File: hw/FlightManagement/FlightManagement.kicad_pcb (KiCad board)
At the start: 2 copper layers, 50 x 50 mm, 116 parts, among them J1 BWSMA-KE-Z001, J2 B4B-EH-A(LF)(SN), J3 B6B-EH-A(LF)(SN), J5 Conn_01x24_MountingPin, J6 Conn_01x02_Socket, J7 Conn_01x02_Pin, U1 YTS1C0033BBG01, U12 TPS54202DDC, U14 SN74LVC1G125DBV, U15 SN74LVC1G125DBV, U2 STM32L431RCTx, U3 MPU-6050, U4 LIS2MDL, U6 XA17-G4K, U8 SN65HVD230, U9 W25Q128JVS, Y1 13.56 MHz, Y2 10.7 MHz, Y3 6.6128 MHz, Y4 Crystal_GND24

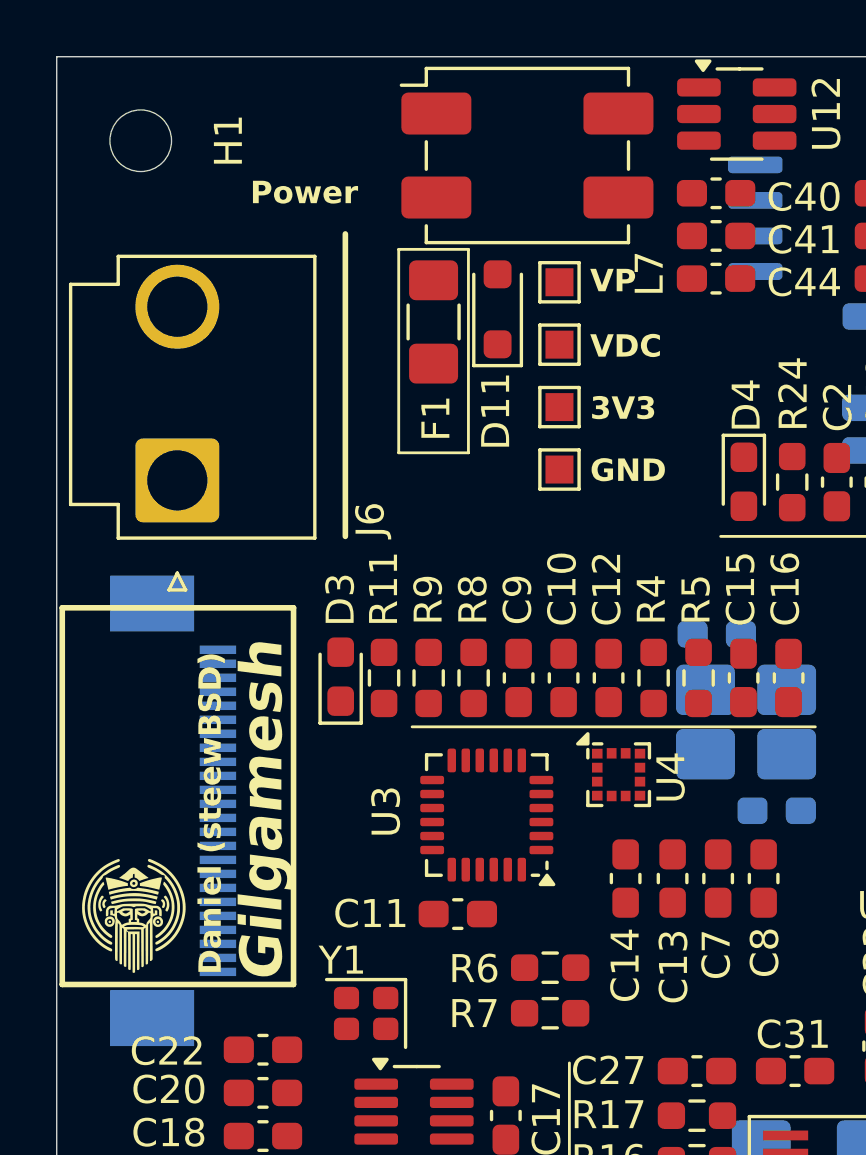
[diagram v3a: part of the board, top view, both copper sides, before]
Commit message: preliminar design for battery power monitor, add sd card to fmu
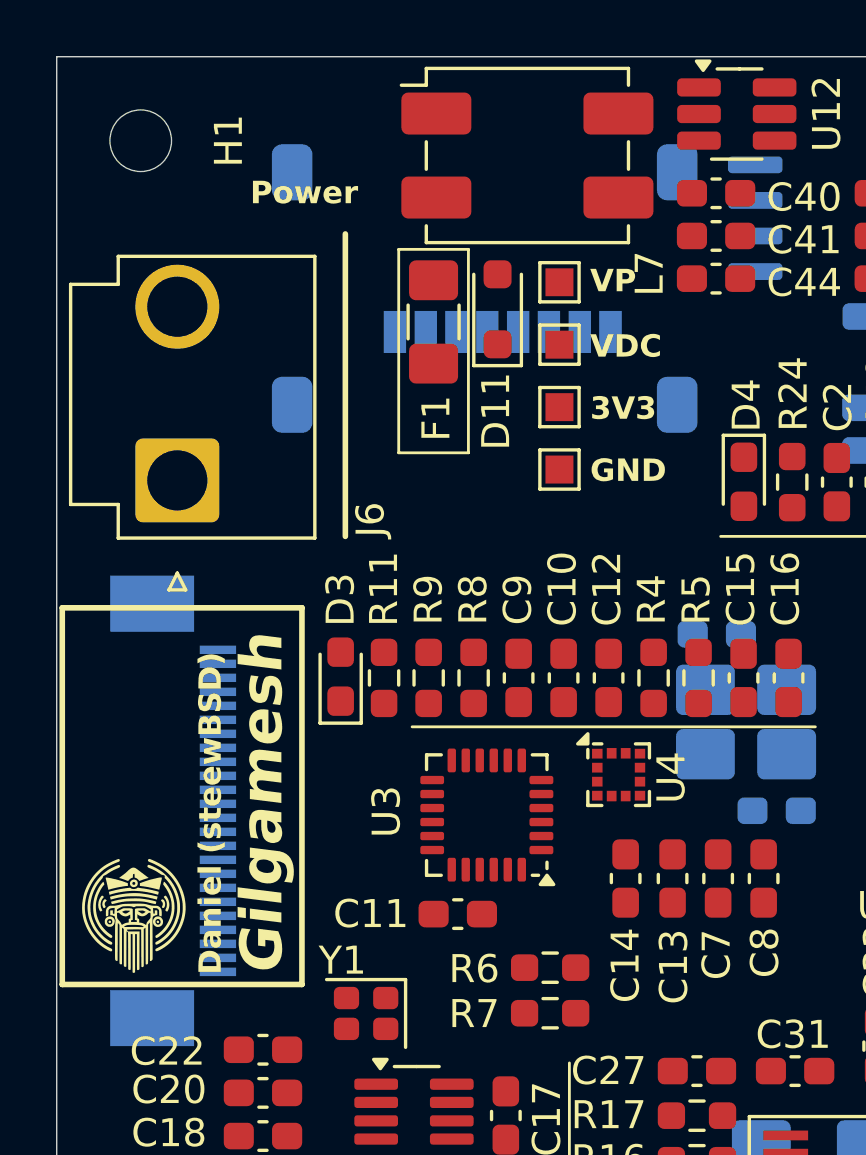
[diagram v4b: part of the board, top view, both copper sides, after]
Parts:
- added J4: Micro_SD_Card, Connector_Card:microSD_HC_Molex_47219-2001, B.Cu at (127.6, 85.2)
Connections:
- U2 pad 10: /AGCDIS -> /CAMERA2
- U2 pad 11: unconnected-(U2-PC3-Pad11) -> /CAMERA3
- U2 pad 14: unconnected-(U2-PA0-Pad14) -> /SDCD
- U2 pad 20: unconnected-(U2-PA4-Pad20) -> /CAMERA1
- U2 pad 21: unconnected-(U2-PA5-Pad21) -> /CAMERA0
- U2 pad 33: /CAMERA3 -> unconnected-(U2-PB12-Pad33)
- U2 pad 34: /CAMERA2 -> /SDSCK
- U2 pad 35: /CAMERA1 -> /SDMISO
- U2 pad 36: /CAMERA0 -> /SDMOSI
- U2 pad 54: unconnected-(U2-PD2-Pad54) -> /AGCDIS

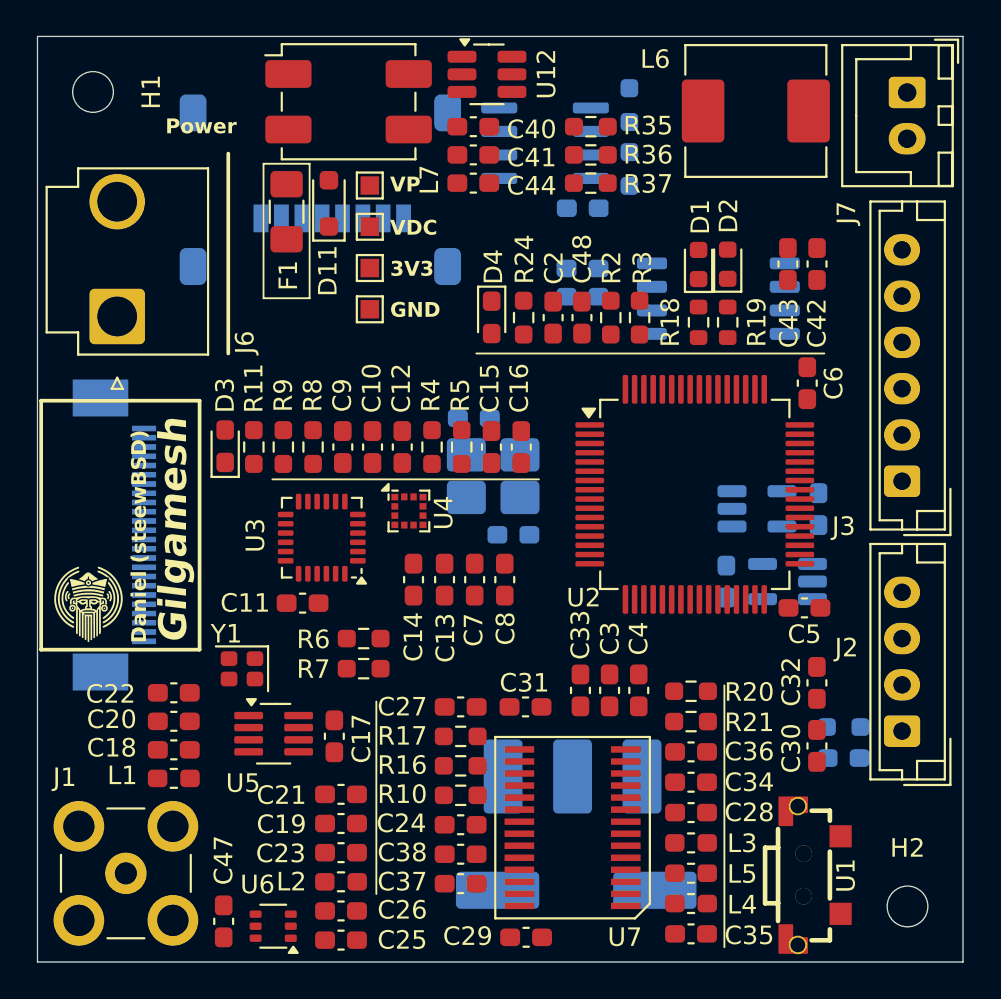
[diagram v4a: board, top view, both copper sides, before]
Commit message: make fmu pcb more organized
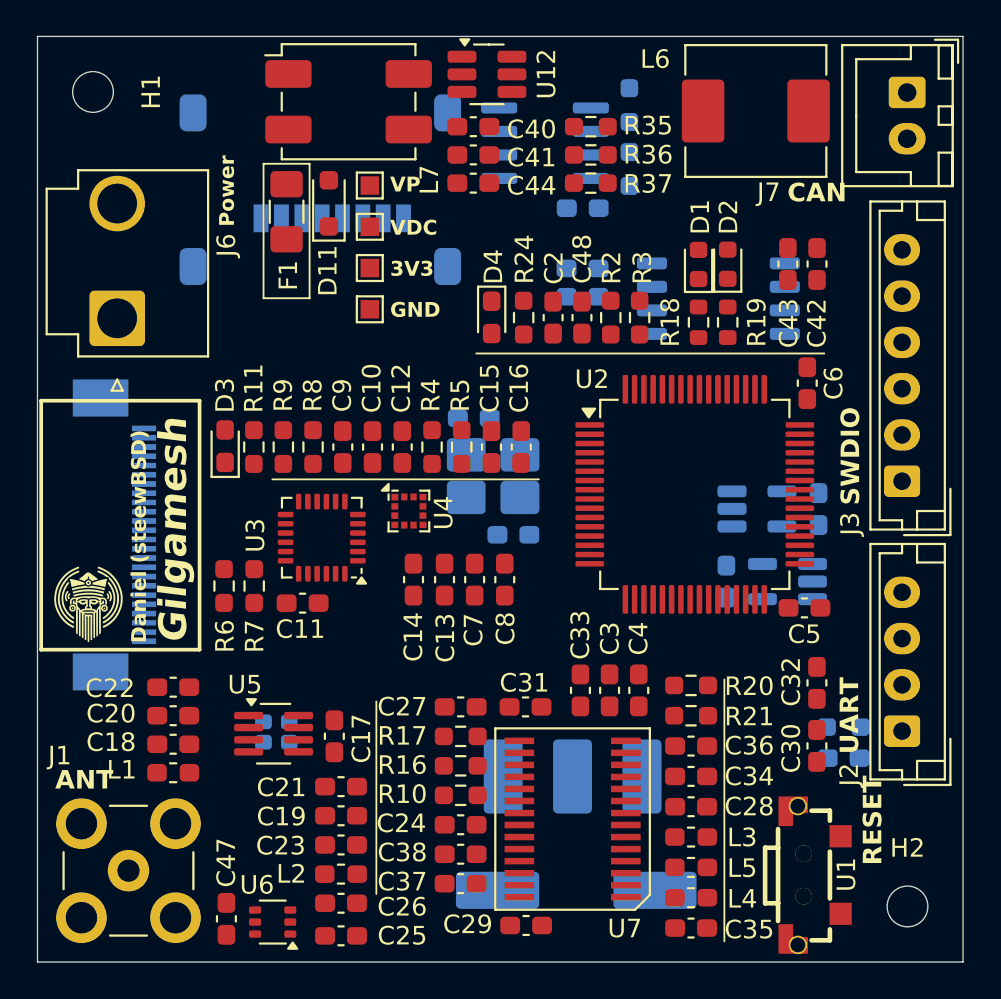
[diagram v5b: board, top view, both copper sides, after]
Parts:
- Y1: moved to B.Cu
- moved R6 8.06 mm to (122.4, 107.2), turned to 90 degrees
- moved R7 7.41 mm to (124.0, 107.2), turned to 90 degrees
- moved Y1 3.89 mm to (125.2, 115.0)
- moved C29 0.64 mm to (138.7, 125.5)
- moved U7 0.47 mm to (141.2, 119.8)
- moved C19 0.42 mm to (128.7, 119.6)
- moved C21 0.42 mm to (128.7, 118.0)
- moved C26 0.42 mm to (128.7, 124.3)
- moved C23 0.42 mm to (128.7, 121.1)
- moved L2 0.42 mm to (128.7, 122.7)
- moved C28 0.31 mm to (147.6, 119.1)
- moved C34 0.31 mm to (147.6, 117.4)
- moved C36 0.31 mm to (147.6, 115.8)
- moved L3 0.31 mm to (147.6, 120.7)
- moved R20 0.31 mm to (147.6, 112.5)
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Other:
- board text added: "ANT"
- board text added: "CAN"
- board text added: "FFC"
- board text added: "MICROSD"
- board text added: "RESET"
- board text added: "SWDIO"
- board text added: "UART"

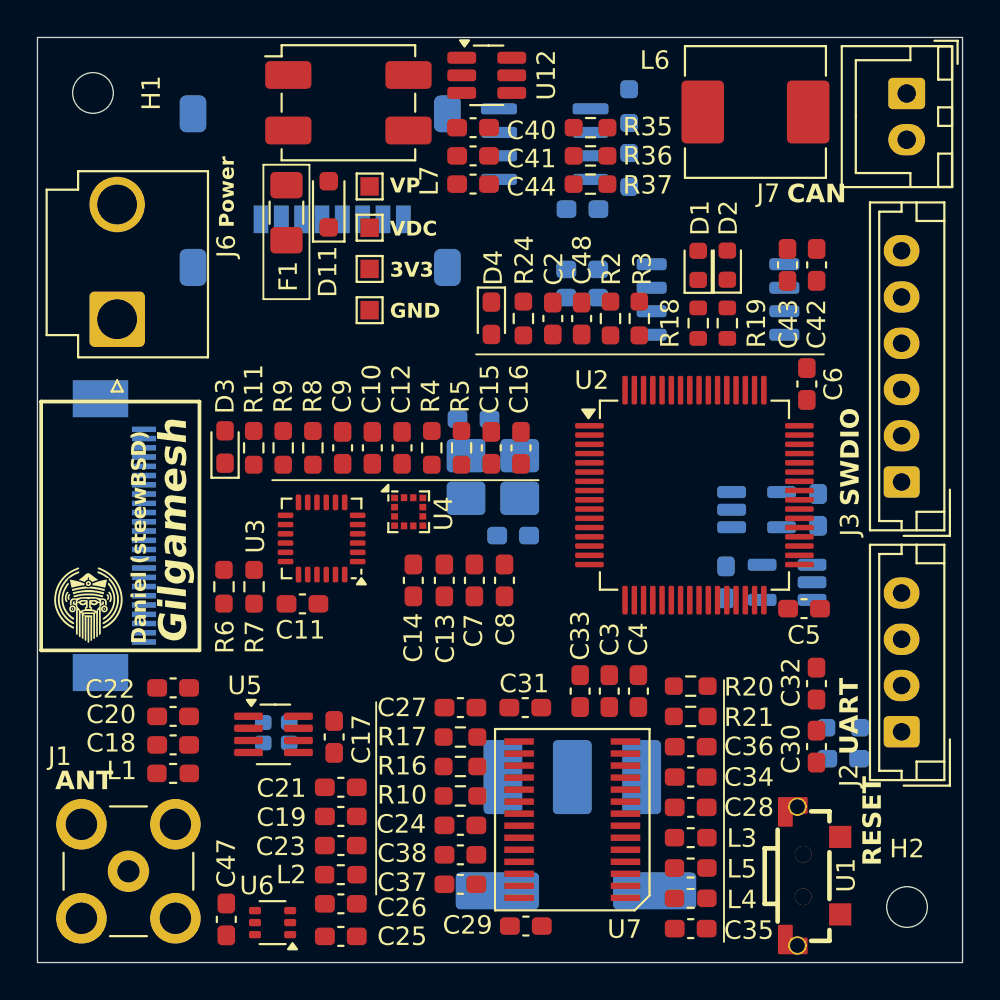
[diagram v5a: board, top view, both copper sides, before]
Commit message: finish fmu routing
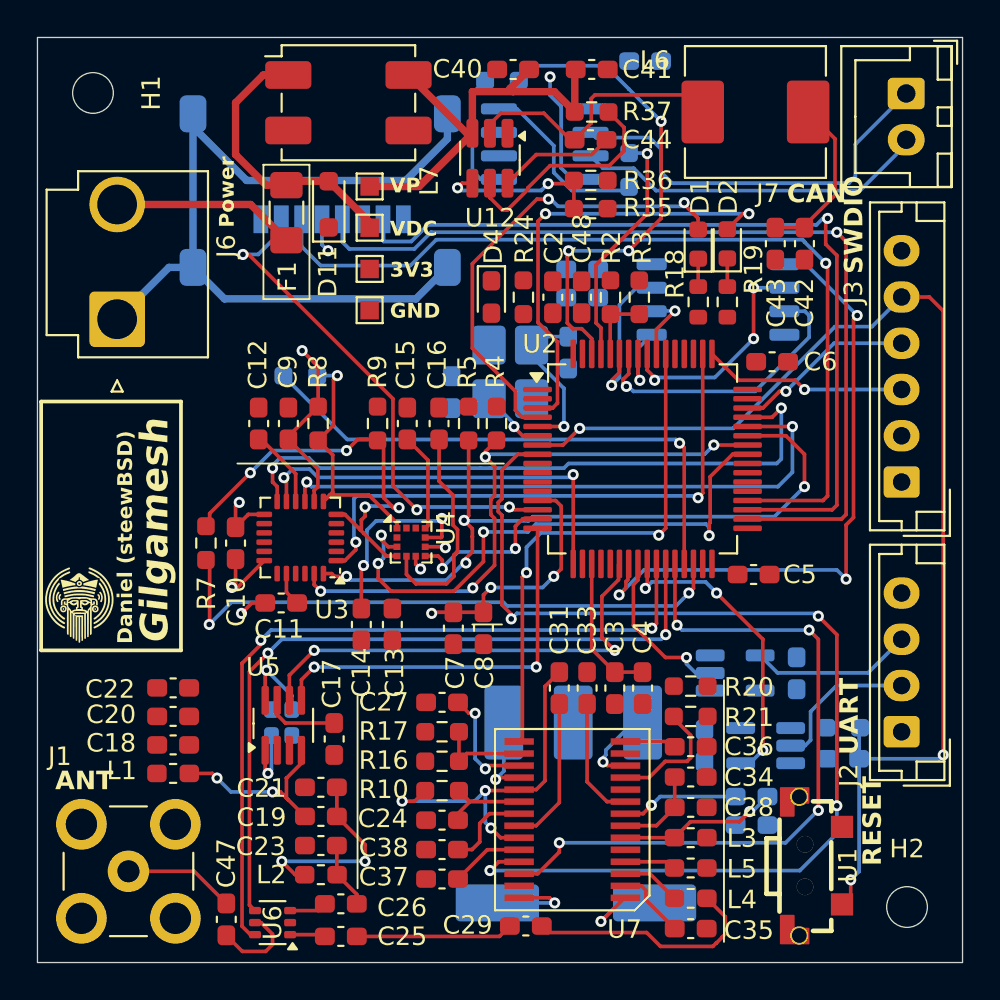
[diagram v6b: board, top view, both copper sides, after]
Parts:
- removed D3: KT-0603W, LED_SMD:LED_0603_1608Metric_Pad1.05x0.95mm_HandSolder
- removed J5: Conn_01x24_MountingPin, Connector_FFC-FPC:Jushuo_AFC07-S24FCA-00_1x24-1MP_P0.50_Horizontal
- removed R11: 1 kOhm, Resistor_SMD:R_0603_1608Metric_Pad0.98x0.95mm_HandSolder
- C30, C32, R6: moved to B.Cu
- moved R6 12.1 mm to (126.5, 95.8), turned to 0 degrees
- moved C10 9.01 mm to (123.0, 104.8), turned to 90 degrees
- moved C50 8.91 mm to (153.3, 111.8)
- moved U14 8.91 mm to (151.7, 115.8)
- moved U15 8.91 mm to (150.0, 111.8)
- moved C49 8.91 mm to (148.3, 115.8)
- moved C39 8.69 mm to (145.1, 78.8)
- moved C46 8.43 mm to (134.7, 96.6), turned to -90 degrees
- moved C41 7.93 mm to (142.2, 79.2)
- moved C12 7.86 mm to (124.2, 98.3)
- moved U5 7.34 mm to (119.9, 114.8), turned to 90 degrees
- moved C32 7.04 mm to (150.9, 118.5), turned to 0 degrees
- moved R12 7.01 mm to (137.4, 79.8), turned to 180 degrees
- moved C44 6.79 mm to (142.2, 83.0)
- moved C45 6.25 mm to (141.0, 94.5), turned to 90 degrees
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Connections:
- net Net-(J6-Pin_2) renamed /VDCPRE
- net Net-(U12-VIN) renamed /VIN
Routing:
- net +3V3: track 0.00 -> 80.6 mm, vias 0 -> 8
- net /NRESET: track 0.00 -> 64.1 mm, vias 0 -> 3
- net /DATAOUT: track 0.00 -> 61.0 mm, vias 0 -> 4
- net /SDSCK: track 0.00 -> 49.4 mm, vias 0 -> 1
- net /SDMOSI: track 0.00 -> 48.4 mm, vias 0 -> 1
- net GNDPWR: track 0.00 -> 46.7 mm
- net /SDMISO: track 0.00 -> 46.4 mm, vias 0 -> 1
- net /RXEN: track 0.00 -> 41.8 mm, vias 0 -> 2
- net /TXEN: track 0.00 -> 40.2 mm, vias 0 -> 2
- net Net-(U2-PA10): track 0.00 -> 39.8 mm, vias 0 -> 4
- net /PDOUT: track 0.00 -> 38.4 mm, vias 0 -> 4
- net /IMU_INT: track 0.00 -> 34.9 mm, vias 0 -> 2
- net /NCS_NOR: track 0.00 -> 34.5 mm, vias 0 -> 3
- net Net-(U2-PA9): track 0.00 -> 32.9 mm, vias 0 -> 4
- net Net-(U2-PA11): track 0.00 -> 32.7 mm, vias 0 -> 2
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- added copper zone on In1.Cu, net +3V3
- added copper zone on In2.Cu, net GND
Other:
- copper layers 2 -> 4

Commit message: FMU completed
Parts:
- C47: renamed from C48; moved to B.Cu
- moved C47 6.14 mm to (143.5, 97.4), turned to 180 degrees
- moved C45 0.27 mm to (141.7, 91.8)
- renumbered C40 to C1, C8 to C10, C10 to C11, C7 to C12, C9 to C13, C22 to C14, C12 to C15, C15 to C16, C14 to C17, C13 to C18, C2 to C19, C41 to C2, C3 to C20, C31 to C21, C5 to C22, C33 to C23, C4 to C24, C6 to C25, C47 to C26, C37 to C27, C29 to C28, C23 to C29, C44 to C3, C21 to C30, C18 to C31, C25 to C32, C24 to C33, C26 to C34, C38 to C35, C19 to C36, C17 to C37, C28 to C38, C36 to C39, C43 to C4, C35 to C40, C34 to C41, C39 to C42, C45 to C43, C51 to C44, C52 to C45, C50 to C46, C46 to C48, C42 to C5, C1 to C50, C30 to C51, C32 to C52, C11 to C6, C27 to C7, C16 to C8, C20 to C9, D11 to D1, D1 to D3, J7 to J1, J6 to J2, J1 to J4, J2 to J5, J4 to J6, L7 to L1, L6 to L2, L1 to L3, L2 to L4, L4 to L5, L3 to L6, L5 to L7, R36 to R1, R21 to R10, R18 to R11, R2 to R12, R19 to R13, R20 to R14, R3 to R15, R17 to R16, R16 to R17, R10 to R18, R13 to R19, R35 to R2, R12 to R20, R6 to R21, R1 to R22, R37 to R3, R9 to R5, R5 to R6, R24 to R8, R8 to R9, TP5 to TP1, TP7 to TP2, TP6 to TP3, TP1 to TP4, U12 to U1, U15 to U10, U9 to U11, U14 to U12, U4 to U2, U2 to U4, U6 to U5, U5 to U6, U1 to U7, U7 to U8, U8 to U9, Y4 to Y1, Y3 to Y2, Y2 to Y3, Y1 to Y4
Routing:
- net GND: track 14.4 -> 165.1 mm, vias 5 -> 49
- net +3V3: track 80.6 -> 187.9 mm, vias 8 -> 43
- net GNDPWR: track 46.7 -> 92.4 mm, vias 0 -> 1
- net Net-(C29-Pad1): track 13.0 -> 15.4 mm
- net /SWCLK: track 11.0 -> 13.3 mm
- net /FSYNC: track 22.2 -> 24.4 mm
- net Net-(D4-K): track 0.00 -> 1.74 mm
- net Net-(U7-IRSEL): track 6.73 -> 8.37 mm
- net Net-(D2-A): track 24.5 -> 26.0 mm
- net Net-(D1-A): track 25.3 -> 25.9 mm
- net /PDOUT: track 38.4 -> 39.1 mm
- added copper zone on B.Cu, net GND
- added copper zone on F.Cu, net GND

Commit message: start working on firmware
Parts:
- renumbered C17 to C11, C8 to C12, C7 to C13, C6 to C14, C16 to C15, C15 to C16, C18 to C17, C14 to C18, C25 to C19, C24 to C20, C23 to C21, C21 to C23, C20 to C24, C19 to C25, C31 to C26, C26 to C27, C27 to C28, C28 to C29, C29 to C30, C30 to C31, C41 to C38, C40 to C39, C39 to C40, C38 to C41, C47 to C43, C43 to C44, C44 to C45, C45 to C47, C52 to C49, C51 to C50, C50 to C51, C49 to C52, C13 to C6, C9 to C7, C12 to C8, C11 to C9, D3 to D2, D2 to D3, R3 to R1, R15 to R10, R14 to R11, R10 to R13, R13 to R14, R11 to R15, R18 to R16, R16 to R18, R1 to R3, R9 to R8, R8 to R9, TP2 to TP1, TP1 to TP2, U3 to U2, U2 to U3
